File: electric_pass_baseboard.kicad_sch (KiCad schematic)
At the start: 9 parts, among them J1 USB_C_Receptacle_USB2.0_16P, J2 Conn_02x05_Odd_Even, J3 Conn_02x05_Odd_Even

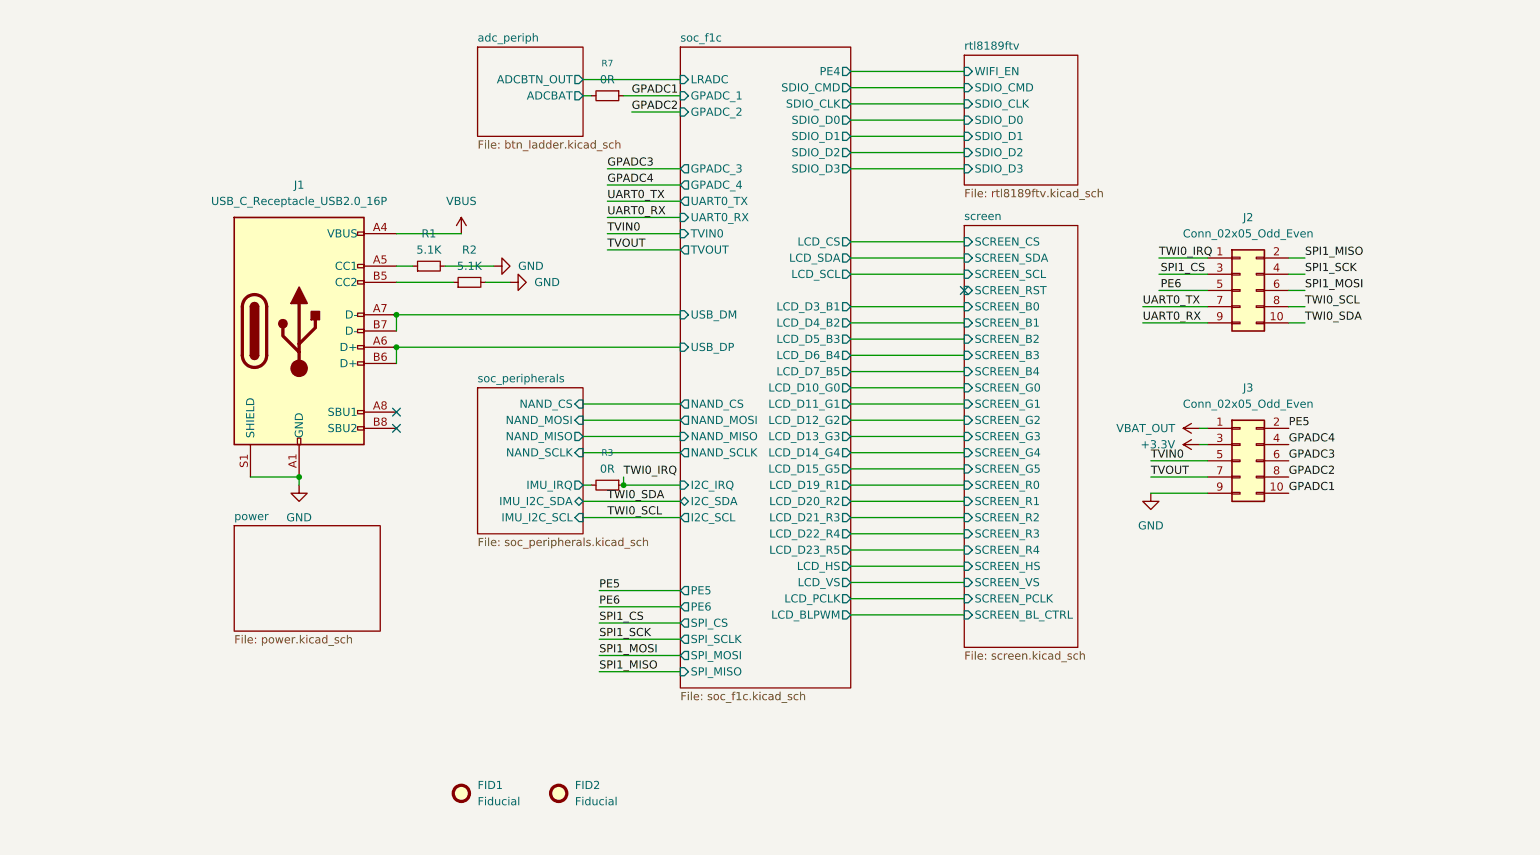
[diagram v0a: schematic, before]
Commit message: V0.3.1 bugfix
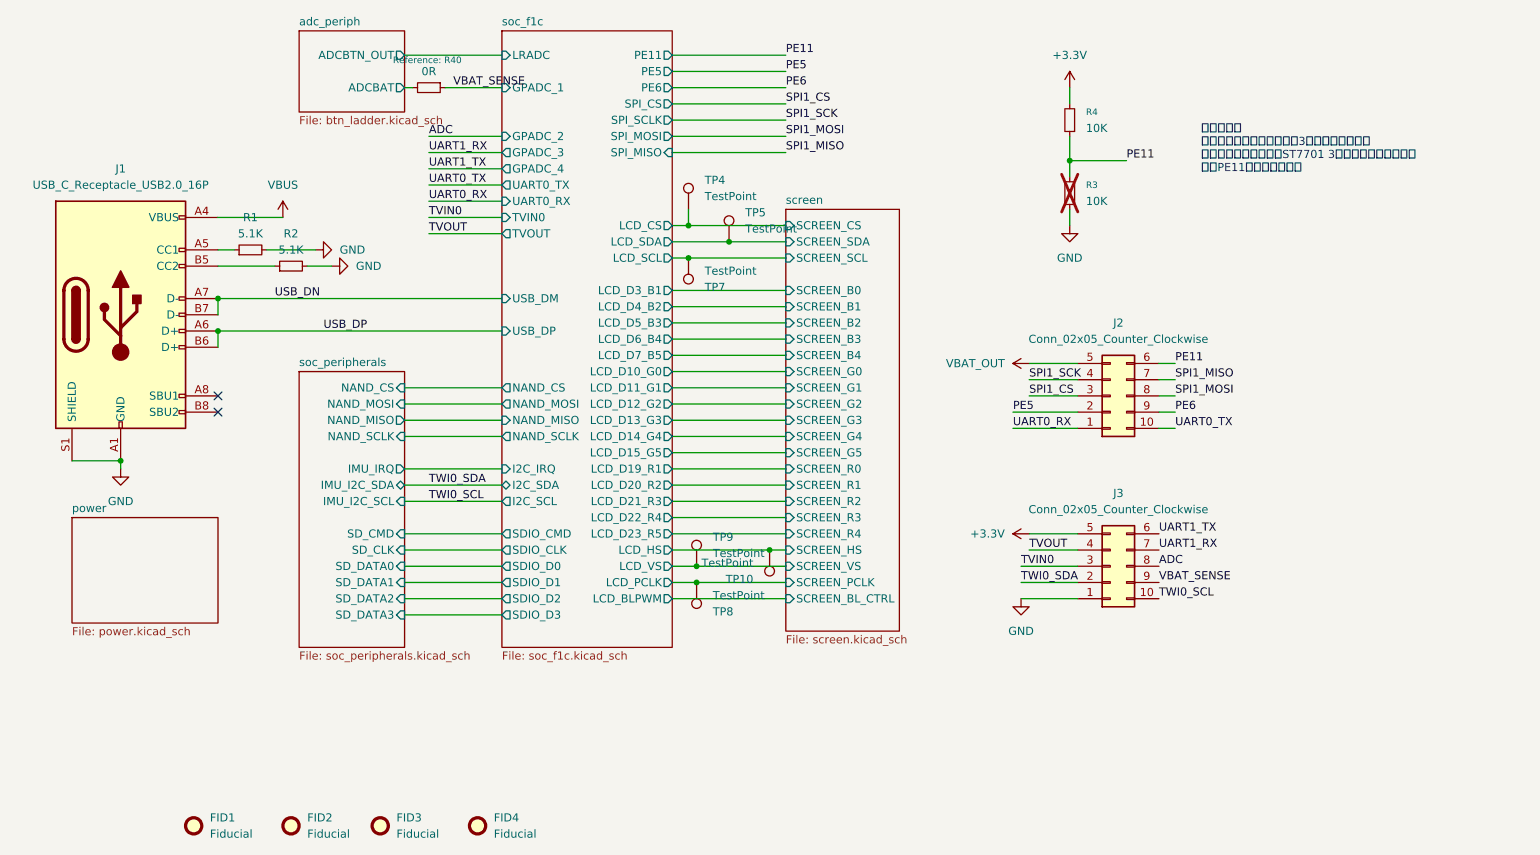
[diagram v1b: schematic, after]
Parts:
- removed J2, J3: Conn_02x05_Odd_Even, Connector_PinSocket_2.54mm:PinSocket_2x05_P2.54mm_Horizontal, symbol Connector_Generic:Conn_02x05_Odd_Even
- removed R7: 0R, Resistor_SMD:R_0603_1608Metric, symbol Device:R_Small
- added FID3, FID4: Fiducial, Fiducial:Fiducial_1mm_Mask2mm, symbol Mechanical:Fiducial
- added J2, J3: Conn_02x05_Counter_Clockwise, EasyEDA:HDR-SMD_10P-P2.54-H-F-R2-C5-W8.5, symbol Connector_Generic:Conn_02x05_Counter_Clockwise
- added R4: 10K, Resistor_SMD:R_0603_1608Metric, symbol Device:R_Small
- added R40: 0R, Resistor_SMD:R_0603_1608Metric, symbol Device:R_Small
- added TP10, TP4, TP5, TP7, TP8, TP9: TestPoint, TestPoint:TestPoint_Pad_D1.5mm, symbol Connector:TestPoint
- R3: value 0R -> 10K; 特殊说明 (none) -> 常规ST7701IPS贴装; now not fitted
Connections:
- net TWI0_IRQ is gone; now on net GND: R3.1
- net +3.3V: now also J3.5 (Pin_5), R4.2
- net GND: now also J3.1 (Pin_1)
- net PE5: now also J2.2 (Pin_2)
- net PE6: now also J2.9 (Pin_9)
- net SPI1_CS: now also J2.3 (Pin_3)
- net SPI1_MISO: now also J2.7 (Pin_7)
- net SPI1_MOSI: now also J2.8 (Pin_8)
- net SPI1_SCK: now also J2.4 (Pin_4)
- net TVIN0: now also J3.3 (Pin_3)
- net TVOUT: now also J3.4 (Pin_4)
- net TWI0_SCL: now also J3.10 (Pin_10)
- net TWI0_SDA: now also J3.2 (Pin_2)
- net UART0_RX: now also J2.1 (Pin_1)
- net UART0_TX: now also J2.10 (Pin_10)
- net VBAT_OUT: now also J2.5 (Pin_5)
- net adc_periph/ADCBAT: now also R40.2
- net screen/SCREEN_CS: now also TP4.1
- net screen/SCREEN_HS: now also TP10.1
- net screen/SCREEN_PCLK: now also TP8.1
- net screen/SCREEN_SCL: now also TP7.1
- net screen/SCREEN_SDA: now also TP5.1
- net screen/SCREEN_VS: now also TP9.1
- net soc_f1c/USB_DM renamed USB_DN
- net soc_f1c/USB_DP renamed USB_DP
- net soc_peripherals/IMU_IRQ renamed PE11
- net PE11: now also J2.6 (Pin_6), R4.1
- new net ADC: J3.8 (Pin_8)
- new net UART1_RX: J3.7 (Pin_7)
- new net UART1_TX: J3.6 (Pin_6)
- new net VBAT_SENSE: J3.9 (Pin_9), R40.1
- no-connect marks 3 -> 2
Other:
- removed sheet rtl8189ftv
- sheet screen ports: added none; removed SCREEN_RST
- sheet soc_f1c ports: added PE11; removed PE4
- sheet soc_peripherals ports: added SD_CLK, SD_CMD, SD_DATA0, SD_DATA1, SD_DATA2, SD_DATA3; removed none
- note added: "配置电阻： 若购买的屏幕是老王电子的3元屏，此处上拉。 若购买的屏幕是通用的ST7701 3寸钢壳屏，此处下拉。 因此PE11请尽量用于输出"
- moved on the sheet: FID1, FID2, J1, R1, R2

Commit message: V0.5
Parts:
- removed R3, R4: 10K, Resistor_SMD:R_0603_1608Metric, symbol Device:R_Small
- added F1: Fuse, Fuse:Fuse_0805_2012Metric, symbol Device:Fuse
- FID1, FID2, FID3, FID4: footprint Fiducial:Fiducial_1mm_Mask2mm -> shirogane:Fiducial_1mm_Mask3mm
- R40: value 0R -> 10R
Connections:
- net VBUS: now also F1.2; no longer J1.A4 (VBUS), J1.A9 (VBUS), J1.B4 (VBUS), J1.B9 (VBUS)
- net PE11 renamed PE3
- new net: F1.1, J1.A4 (VBUS), J1.A9 (VBUS), J1.B4 (VBUS), J1.B9 (VBUS)
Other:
- sheet power ports: added PWR_SHUTDOWN; removed none
- sheet soc_f1c ports: added PE3, PWR_SHUTDOWN; removed I2C_IRQ, PE11
- sheet soc_peripherals ports: added none; removed IMU_I2C_SCL, IMU_I2C_SDA, IMU_IRQ
- note added: "贴10R省一种料"
- note removed: "配置电阻： 若购买的屏幕是老王电子的3元屏，此处上拉。 若购买的屏幕是通用的ST7701 3寸钢壳屏，此处下拉。 因此PE11请尽量用于输出"
- moved on the sheet: Reference: R40
